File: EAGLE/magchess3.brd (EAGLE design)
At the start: 49.5 x 40.6 mm, 14 parts

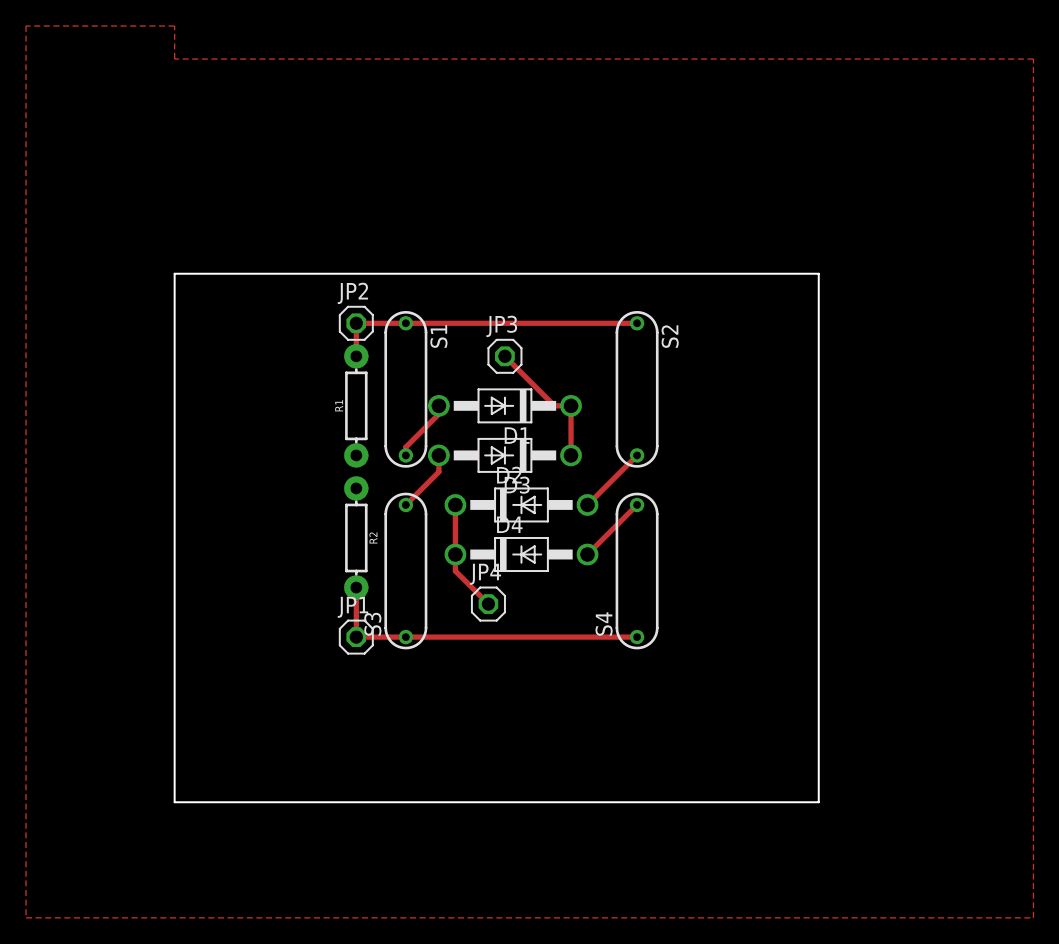
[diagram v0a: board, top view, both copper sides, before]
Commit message: figured out how to work around relaly small garbage
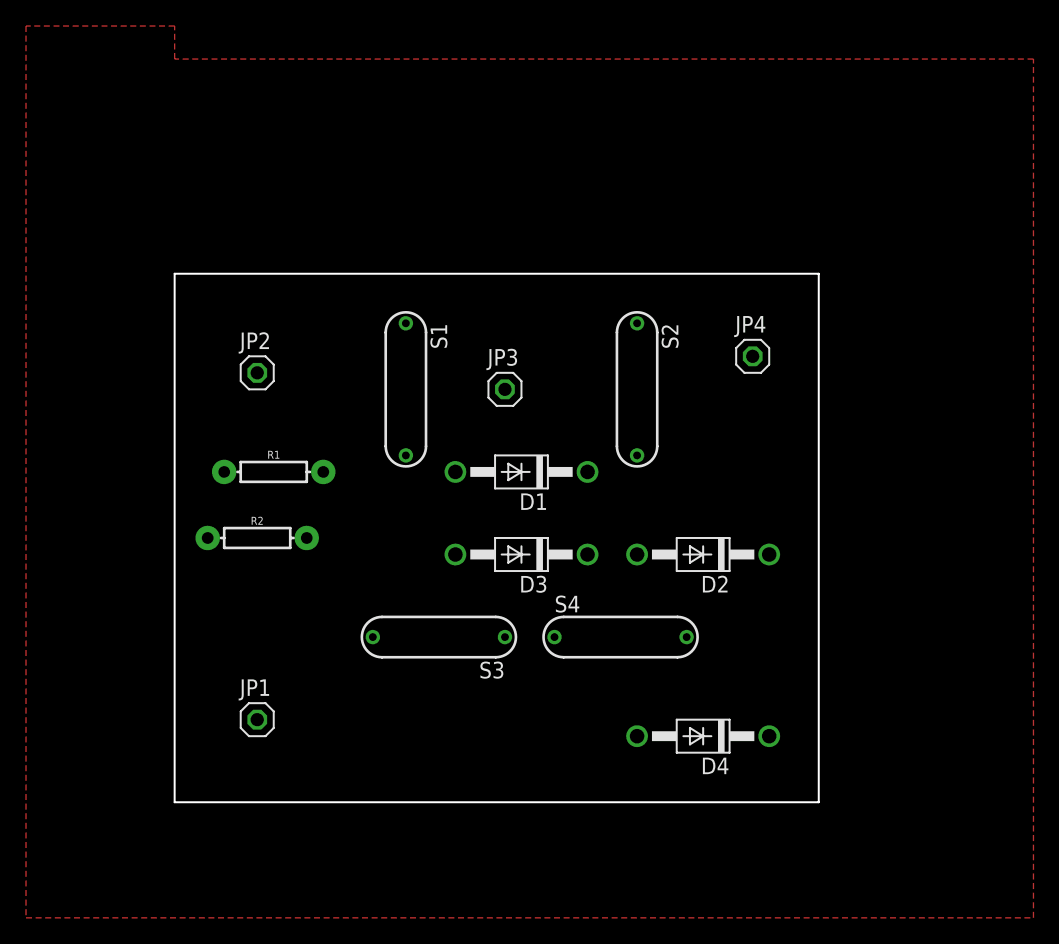
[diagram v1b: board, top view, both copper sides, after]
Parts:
- moved JP4 27.9 mm to (62.2, 48.3)
- moved D4 19.8 mm to (58.4, 19.1), turned to 180 degrees
- moved D2 14.5 mm to (58.4, 33.0), turned to 180 degrees
- moved JP1 9.92 mm to (24.1, 20.3)
- moved JP2 8.52 mm to (24.1, 47.0)
- moved R1 8.13 mm to (25.4, 39.4), turned to 0 degrees
- moved D3 7.73 mm to (44.5, 33.0)
- moved R2 7.62 mm to (24.1, 34.3), turned to 0 degrees
- moved S3 5.68 mm to (38.1, 26.7), turned to 180 degrees
- moved D1 5.24 mm to (44.5, 39.4)
- moved S4 5.24 mm to (52.1, 26.7), turned to 0 degrees
- moved JP3 2.54 mm to (43.2, 45.7)
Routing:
- net N$2: track 25.4 -> 0.00 mm
- net N$1: track 24.1 -> 0.00 mm
- net N$8: track 10.5 -> 0.00 mm
- net N$7: track 8.67 -> 0.00 mm
- net N$6: track 5.39 -> 0.00 mm
- net N$5: track 5.39 -> 0.00 mm
- net N$4: track 4.86 -> 0.00 mm
- net N$3: track 4.86 -> 0.00 mm
